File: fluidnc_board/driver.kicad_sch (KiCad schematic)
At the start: 46 parts, among them J3 Screw_Terminal_01x02, J4 Conn_01x06_Female, J5 SWD, J6 Screw_Terminal_01x04, Q1 IRF7809AVTRPBF, SW1 SW_Push, U2 ADG3304, U3 HCPL-0630, U4 STM32F103C8Tx, U5 TMC5160_SILENTSTEPSTICK, Y1 8M

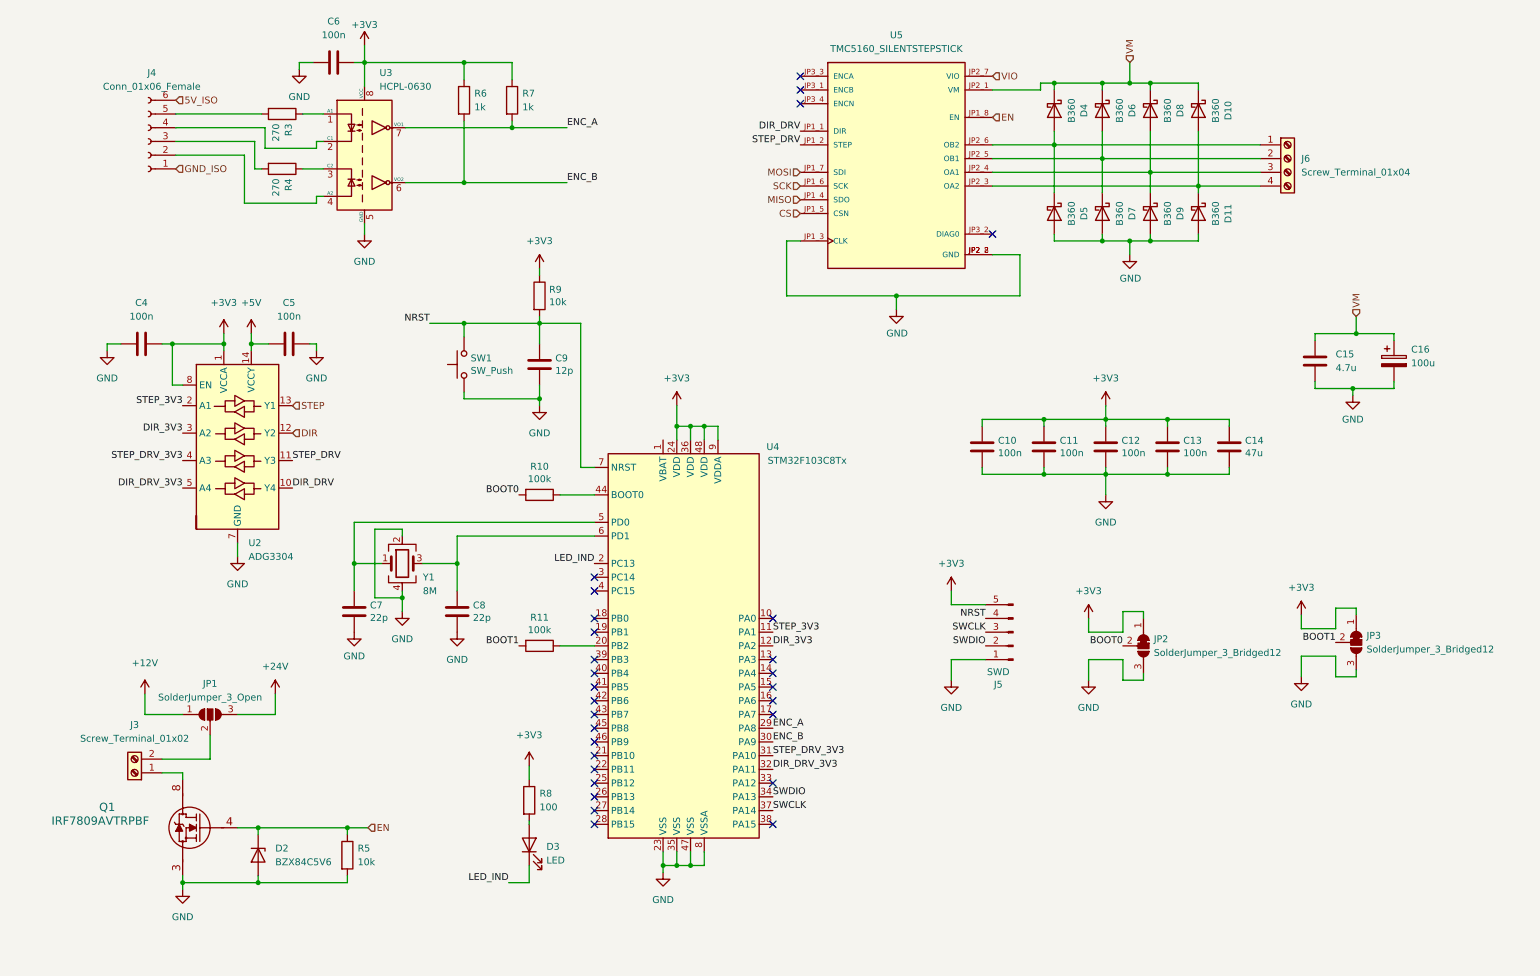
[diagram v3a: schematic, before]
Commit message: fixed some footprint associations, placed footprints
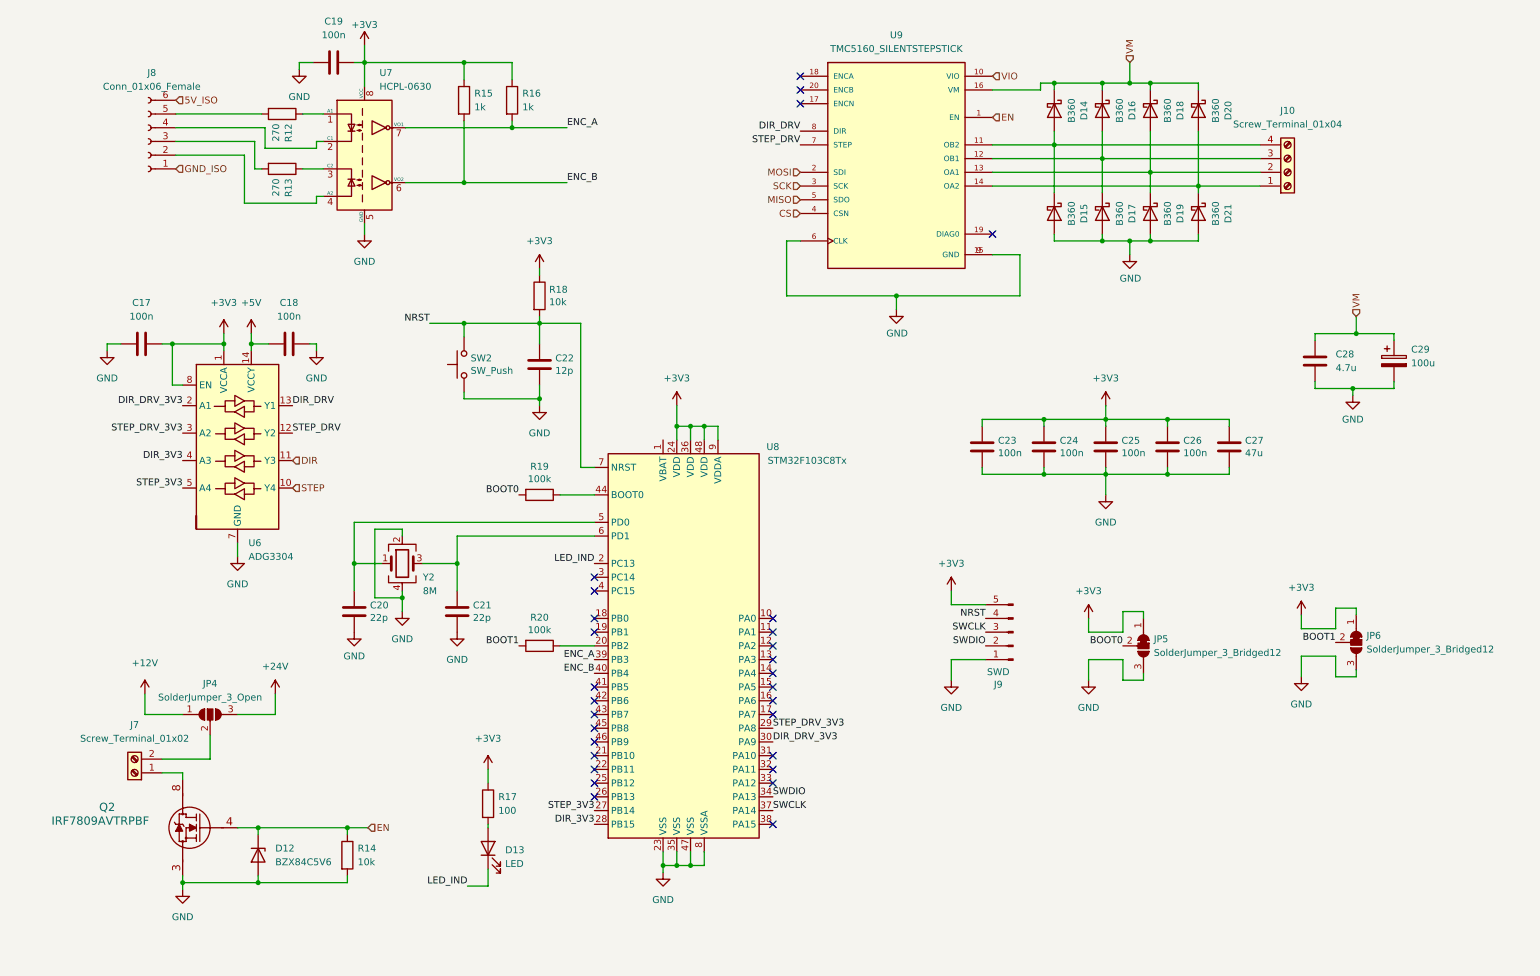
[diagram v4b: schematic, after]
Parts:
- C17: renamed from C4; footprint Capacitor_SMD:C_0603_1608Metric_Pad1.05x0.95mm_HandSolder -> Capacitor_SMD:C_0603_1608Metric_Pad1.08x0.95mm_HandSolder; Digikey Part No. 1276-1941-1-ND -> (none)
- C18: renamed from C5; footprint Capacitor_SMD:C_0603_1608Metric_Pad1.05x0.95mm_HandSolder -> Capacitor_SMD:C_0603_1608Metric_Pad1.08x0.95mm_HandSolder; Digikey Part No. 1276-1941-1-ND -> (none)
- C19: renamed from C6; footprint Capacitor_SMD:C_0603_1608Metric_Pad1.05x0.95mm_HandSolder -> Capacitor_SMD:C_0603_1608Metric_Pad1.08x0.95mm_HandSolder; Digikey Part No. 1276-1941-1-ND -> (none)
- C20: renamed from C7; Digikey Part No. 1276-2228-1-ND -> (none)
- C21: renamed from C8; Digikey Part No. 1276-2228-1-ND -> (none)
- C22: renamed from C9; Digikey Part No. 1276-6640-1-ND -> (none)
- C23: renamed from C10; footprint Capacitor_SMD:C_0603_1608Metric_Pad1.05x0.95mm_HandSolder -> Capacitor_SMD:C_0603_1608Metric_Pad1.08x0.95mm_HandSolder; Digikey Part No. 1276-1941-1-ND -> (none)
- C24: renamed from C11; footprint Capacitor_SMD:C_0603_1608Metric_Pad1.05x0.95mm_HandSolder -> Capacitor_SMD:C_0603_1608Metric_Pad1.08x0.95mm_HandSolder; Digikey Part No. 1276-1941-1-ND -> (none)
- C25: renamed from C12; footprint Capacitor_SMD:C_0603_1608Metric_Pad1.05x0.95mm_HandSolder -> Capacitor_SMD:C_0603_1608Metric_Pad1.08x0.95mm_HandSolder; Digikey Part No. 1276-1941-1-ND -> (none)
- C26: renamed from C13; footprint Capacitor_SMD:C_0603_1608Metric_Pad1.05x0.95mm_HandSolder -> Capacitor_SMD:C_0603_1608Metric_Pad1.08x0.95mm_HandSolder; Digikey Part No. 1276-1941-1-ND -> (none)
- C27: renamed from C14; Digikey Part No. 1276-1852-1-ND -> (none)
- C28: renamed from C15; Digikey Part No. 1276-1248-1-ND -> (none)
- C29: renamed from C16; Digikey Part No. UCD1H101MCL6CT-ND -> (none)
- D12: renamed from D2; Digikey Part No. 1514-BZX84C5V6TRPBFREECT-ND -> (none)
- D13: renamed from D3; Digikey Part No. 160-1456-1-ND -> (none)
- D14: renamed from D4; footprint Diode_SMD:D_SMA_Handsoldering -> Diode_SMD:D_SMC; Digikey Part No. CD214A-B360RCT-ND -> (none)
- D15: renamed from D5; footprint Diode_SMD:D_SMA_Handsoldering -> Diode_SMD:D_SMC; Digikey Part No. CD214A-B360RCT-ND -> (none)
- D16: renamed from D6; footprint Diode_SMD:D_SMA_Handsoldering -> Diode_SMD:D_SMC; Digikey Part No. CD214A-B360RCT-ND -> (none)
- D17: renamed from D7; footprint Diode_SMD:D_SMA_Handsoldering -> Diode_SMD:D_SMC; Digikey Part No. CD214A-B360RCT-ND -> (none)
- D18: renamed from D8; footprint Diode_SMD:D_SMA_Handsoldering -> Diode_SMD:D_SMC; Digikey Part No. CD214A-B360RCT-ND -> (none)
- D19: renamed from D9; footprint Diode_SMD:D_SMA_Handsoldering -> Diode_SMD:D_SMC; Digikey Part No. CD214A-B360RCT-ND -> (none)
- D20: renamed from D10; footprint Diode_SMD:D_SMA_Handsoldering -> Diode_SMD:D_SMC; Digikey Part No. CD214A-B360RCT-ND -> (none)
- D21: renamed from D11; footprint Diode_SMD:D_SMA_Handsoldering -> Diode_SMD:D_SMC; Digikey Part No. CD214A-B360RCT-ND -> (none)
- Q2: renamed from Q1; Digikey Part No. IRF7809AVPBFCT-ND -> (none)
- R12: renamed from R3; footprint Resistor_SMD:R_0805_2012Metric_Pad1.15x1.40mm_HandSolder -> Resistor_SMD:R_1206_3216Metric_Pad1.30x1.75mm_HandSolder; Digikey Part No. 311-.27LUCT-ND -> (none)
- R13: renamed from R4; footprint Resistor_SMD:R_0805_2012Metric_Pad1.15x1.40mm_HandSolder -> Resistor_SMD:R_1206_3216Metric_Pad1.30x1.75mm_HandSolder; Digikey Part No. 311-.27LUCT-ND -> (none)
- R14: renamed from R5; Digikey Part No. 311-10KARCT-ND -> (none)
- R15: renamed from R6; Digikey Part No. 311-1.00KFRCT-ND -> (none)
- R16: renamed from R7; Digikey Part No. 311-1.00KFRCT-ND -> (none)
- R17: renamed from R8; footprint Resistor_SMD:R_0603_1608Metric_Pad0.98x0.95mm_HandSolder -> Resistor_SMD:R_1206_3216Metric_Pad1.30x1.75mm_HandSolder; Digikey Part No. 311-100GRCT-ND -> (none)
- R18: renamed from R9; Digikey Part No. 311-10KARCT-ND -> (none)
- R19: renamed from R10; Digikey Part No. 311-100KGRCT-ND -> (none)
- R20: renamed from R11; Digikey Part No. 311-100KGRCT-ND -> (none)
- SW2: renamed from SW1; Digikey Part No. EG2526CT-ND -> (none)
- U6: renamed from U2; Digikey Part No. 505-ADG3304BRUZ-ND -> (none)
- U7: renamed from U3; Digikey Part No. 516-1487-1-ND -> (none)
- U8: renamed from U4; Digikey Part No. 497-6063-ND -> (none)
- U9: renamed from U5; MANUFACTURER (none) -> Trinamic; MAXIMUM_PACKAGE_HEIGHT (none) -> N/A; PARTREV (none) -> v11; STANDARD (none) -> Manufacturer Recommendations
- Y2: renamed from Y1; Digikey Part No. 50-ECS-80-18-33-JGN-CT-ND -> (none)
- renumbered J6 to J10, J3 to J7, J4 to J8, J5 to J9, JP1 to JP4, JP2 to JP5, JP3 to JP6
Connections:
- net CS: now also U9.4 (CSN); no longer U9.JP1_5 (CSN)
- net DIR: now also U6.11 (Y3); no longer U6.12 (Y2)
- net DIR_3V3: now also U6.4 (A3), U8.28 (PB15); no longer U6.3 (A2), U8.12 (PA2)
- net DIR_DRV: now also U6.13 (Y1), U9.8 (DIR); no longer U6.10 (Y4), U9.JP1_1 (DIR)
- net DIR_DRV_3V3: now also U6.2 (A1), U8.30 (PA9); no longer U6.5 (A4), U8.32 (PA11)
- net EN: now also U9.1 (EN); no longer U9.JP1_8 (EN)
- net ENC_A: now also U8.39 (PB3); no longer U8.29 (PA8)
- net ENC_B: now also U8.40 (PB4); no longer U8.30 (PA9)
- net GND: now also U9.15 (GND), U9.6 (CLK), U9.9 (GND); no longer U9.JP1_3 (CLK), U9.JP2_2 (GND), U9.JP2_8 (GND)
- net MISO: now also U9.5 (SDO); no longer U9.JP1_4 (SDO)
- net MOSI: now also U9.2 (SDI); no longer U9.JP1_7 (SDI)
- net SCK: now also U9.3 (SCK); no longer U9.JP1_6 (SCK)
- net STEP: now also U6.10 (Y4); no longer U6.13 (Y1)
- net STEP_3V3: now also U6.5 (A4), U8.27 (PB14); no longer U6.2 (A1), U8.11 (PA1)
- net STEP_DRV: now also U6.12 (Y2), U9.7 (STEP); no longer U6.11 (Y3), U9.JP1_2 (STEP)
- net STEP_DRV_3V3: now also U6.3 (A2), U8.29 (PA8); no longer U6.4 (A3), U8.31 (PA10)
- net VIO: now also U9.10 (VIO); no longer U9.JP2_7 (VIO)
- net VM: now also U9.16 (VM); no longer U9.JP2_1 (VM)
- net at D14.2 (A), D15.1 (K): now also J10.4 (Pin_4), U9.11 (OB2); no longer J10.1 (Pin_1), U9.JP2_6 (OB2)
- net at D16.2 (A), D17.1 (K): now also J10.3 (Pin_3), U9.12 (OB1); no longer J10.2 (Pin_2), U9.JP2_5 (OB1)
- net at D18.2 (A), D19.1 (K): now also J10.2 (Pin_2), U9.13 (OA1); no longer J10.3 (Pin_3), U9.JP2_4 (OA1)
- net at D20.2 (A), D21.1 (K): now also J10.1 (Pin_1), U9.14 (OA2); no longer J10.4 (Pin_4), U9.JP2_3 (OA2)
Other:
- moved on the sheet: D13, R17

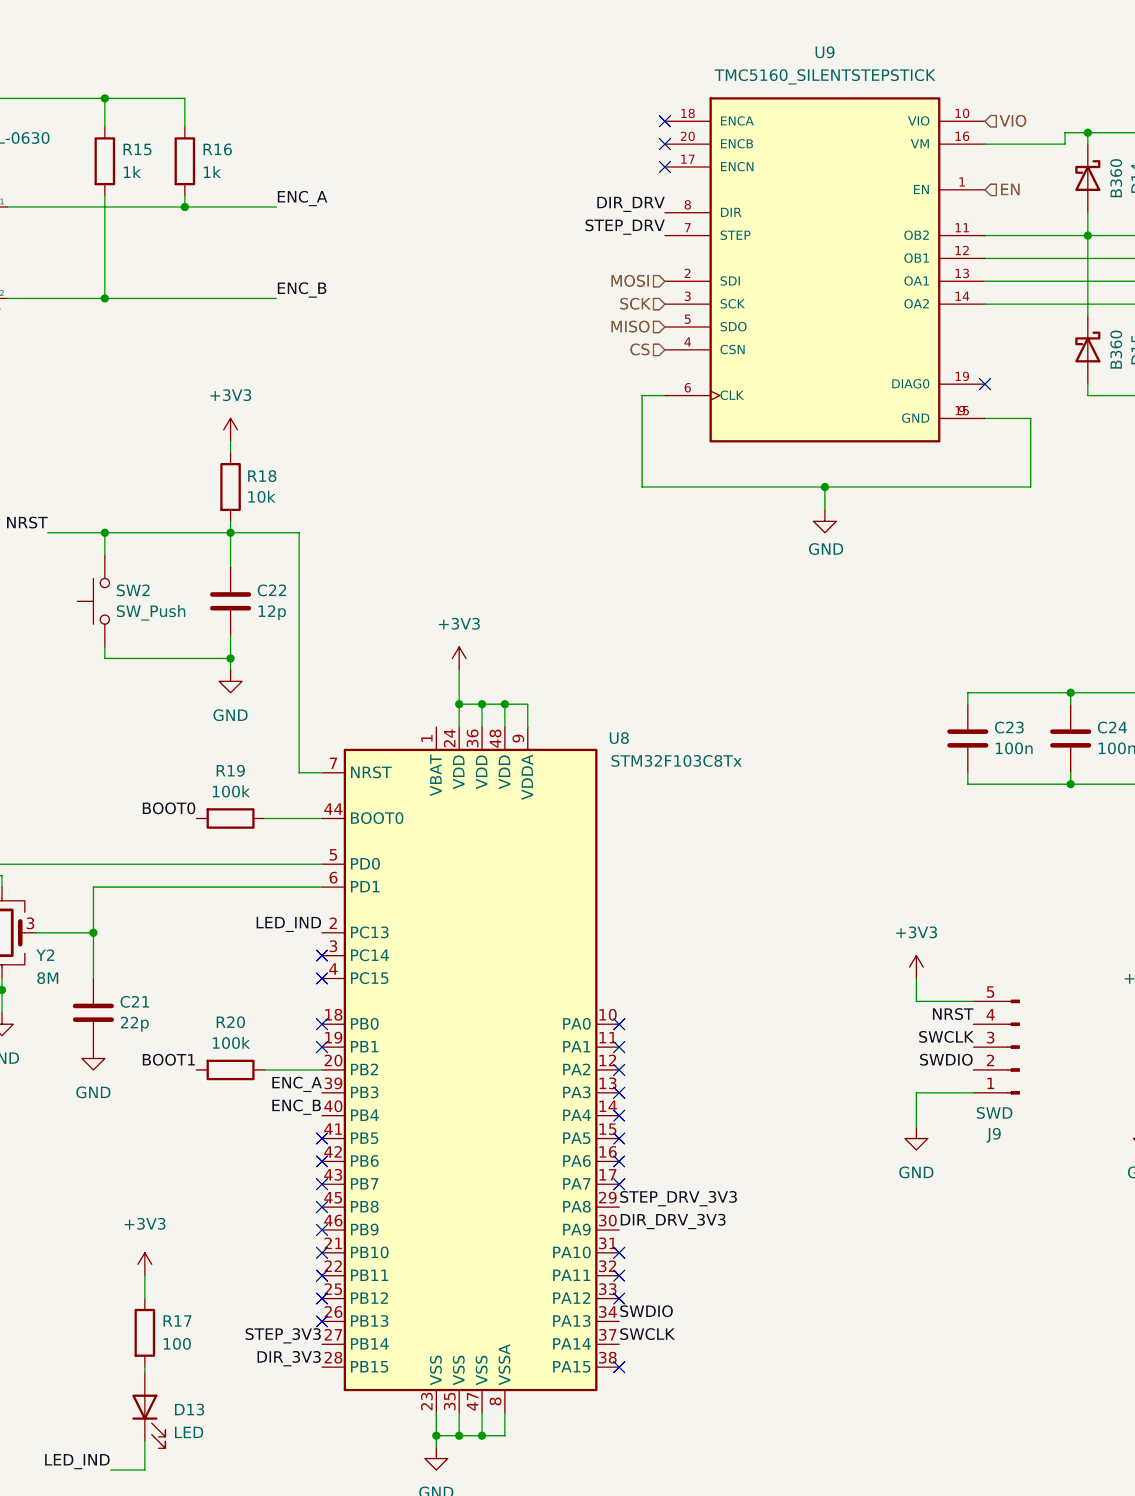
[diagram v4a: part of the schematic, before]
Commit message: placed and routed one stepper motor unit
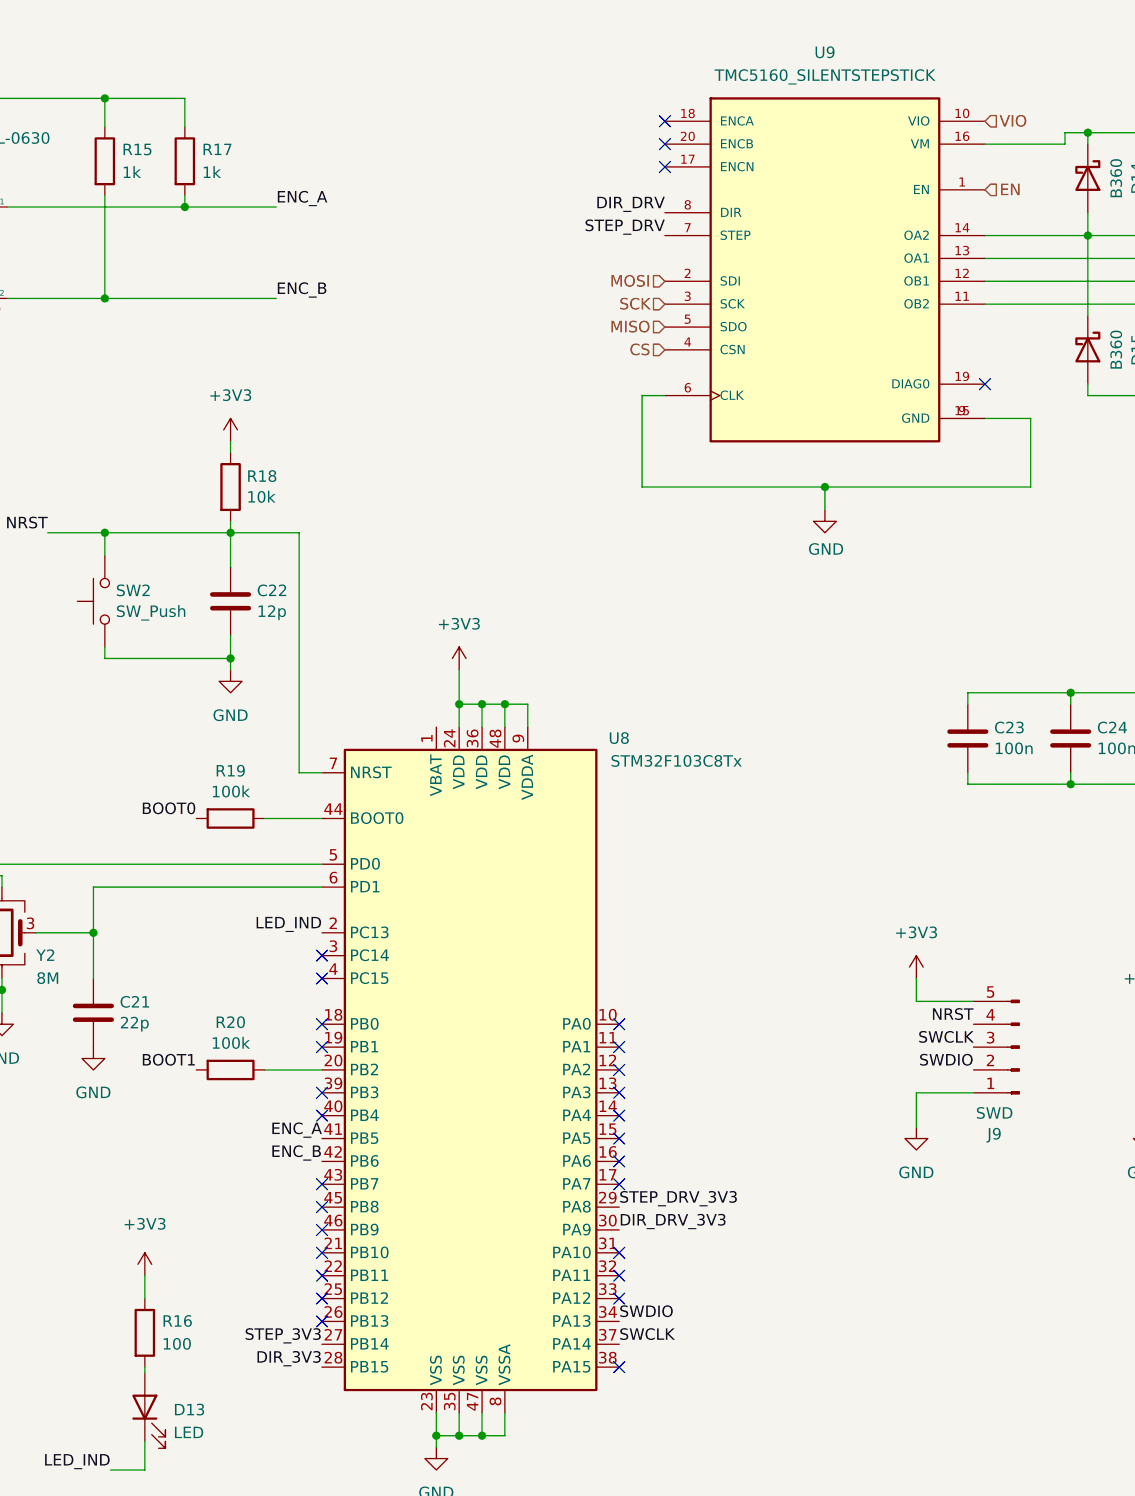
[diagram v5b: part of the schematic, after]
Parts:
- C29: Digikey Part No. (none) -> UCD1H101MCL6CT-ND
- renumbered R17 to R16, R16 to R17
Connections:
- net ENC_A: now also U8.41 (PB5); no longer U8.39 (PB3)
- net ENC_B: now also U8.42 (PB6); no longer U8.40 (PB4)
- net at D14.2 (A), D15.1 (K), J10.4 (Pin_4): now also U9.14 (OA2); no longer U9.11 (OB2)
- net at D20.2 (A), D21.1 (K), J10.1 (Pin_1): now also U9.11 (OB2); no longer U9.14 (OA2)
- net at D18.2 (A), D19.1 (K), J10.2 (Pin_2): now also U9.12 (OB1); no longer U9.13 (OA1)
- net at D16.2 (A), D17.1 (K), J10.3 (Pin_3): now also U9.13 (OA1); no longer U9.12 (OB1)
